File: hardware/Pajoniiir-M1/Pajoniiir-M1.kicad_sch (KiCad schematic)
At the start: 0 parts

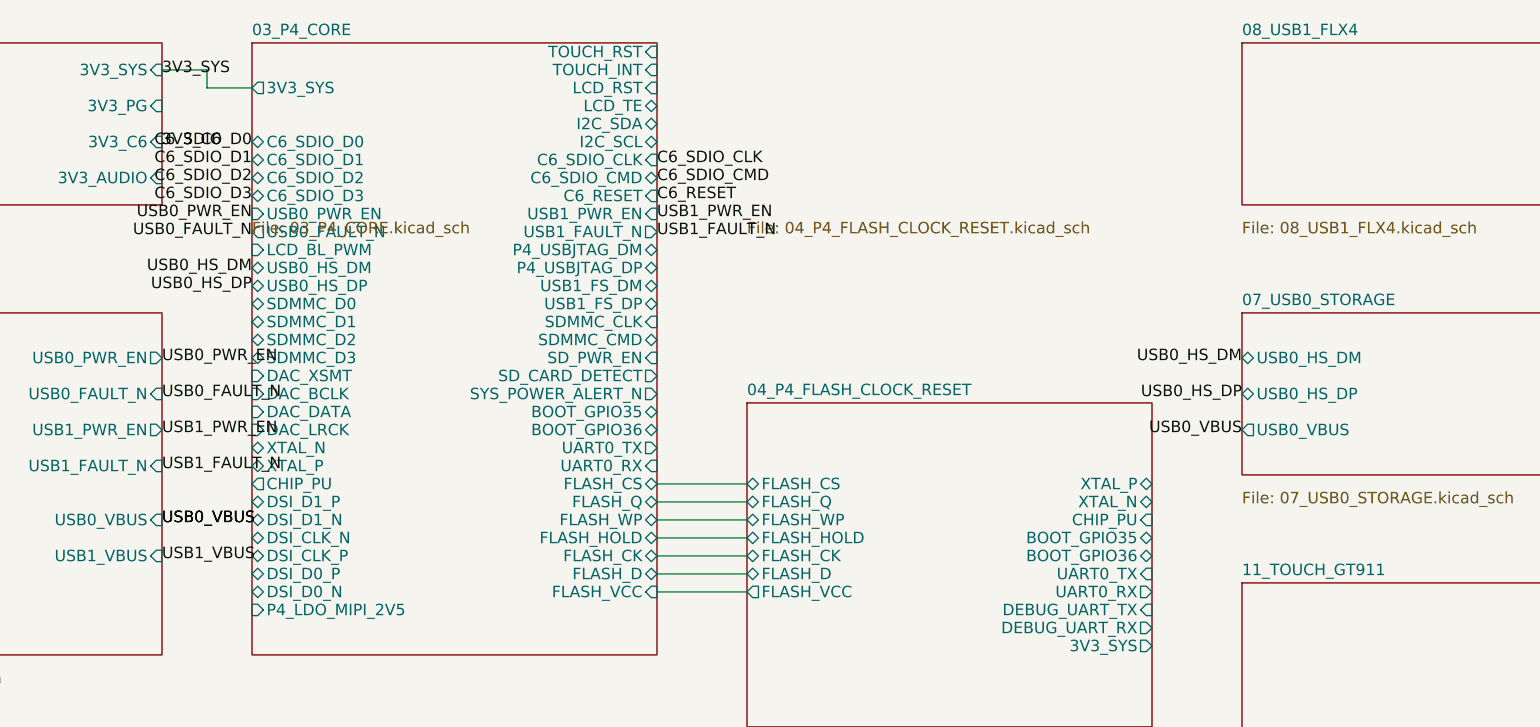
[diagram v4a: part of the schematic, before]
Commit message: hardware: wire USB1 FLX4 hierarchy
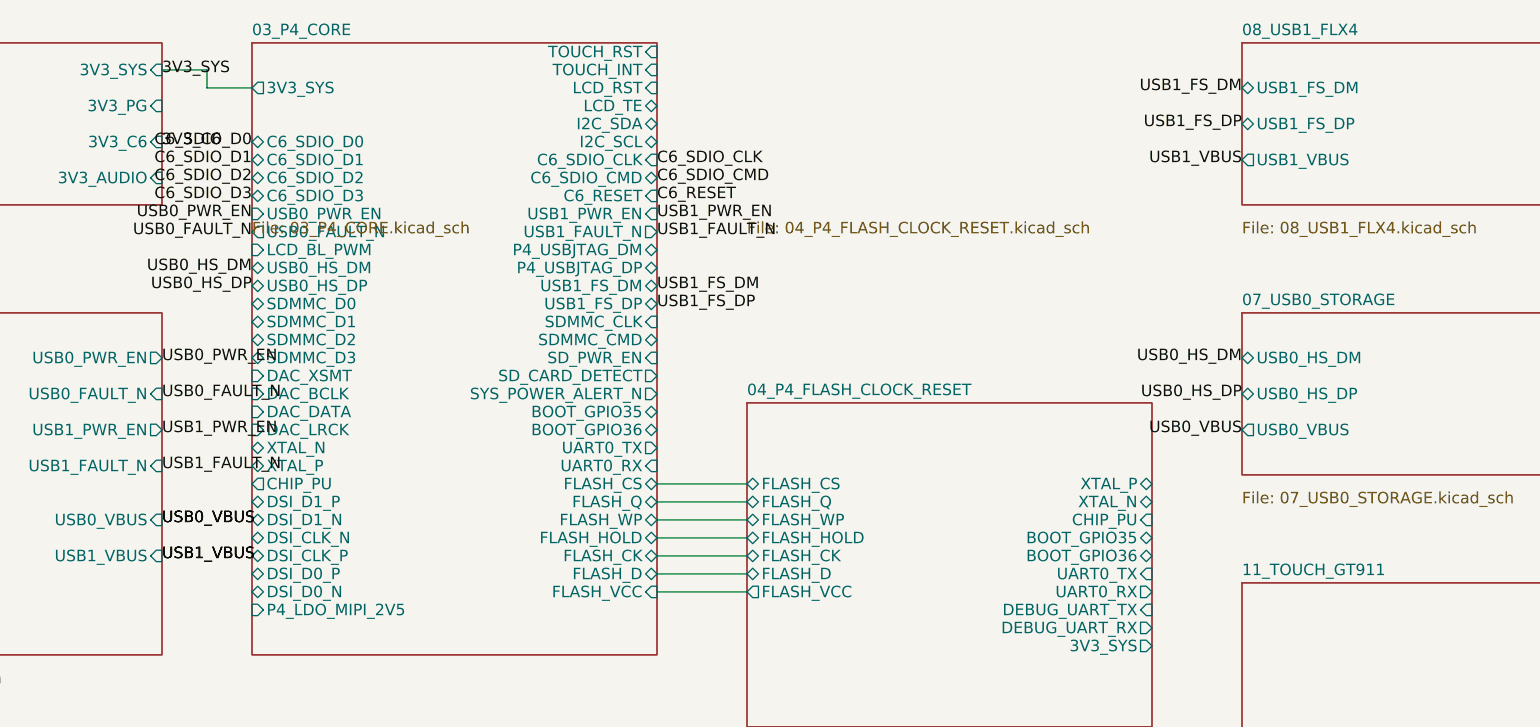
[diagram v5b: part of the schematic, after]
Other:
- sheet 08_USB1_FLX4 ports: added USB1_FS_DM, USB1_FS_DP, USB1_VBUS; removed none
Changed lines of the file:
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@@
       (effects (font (size 1.27 1.27)) (justify left top))
     )
+    (pin "USB1_FS_DM" bidirectional (at 240 25 180) (effects (font (size 1.27 1.27)) (justify left)))
+    (pin "USB1_FS_DP" bidirectional (at 240 29 180) (effects (font (size 1.27 1.27)) (justify left)))
+    (pin "USB1_VBUS" output (at 240 33 180) (effects (font (size 1.27 1.27)) (justify left)))
     (instances
       (project "Pajoniiir-M1"
@@
   (label "USB0_HS_DP" (at 130 47 180) (effects (font (size 1.27 1.27))))
   (label "USB0_VBUS" (at 120 73 0) (effects (font (size 1.27 1.27))))
+  (label "USB1_FS_DM" (at 240 25 180) (effects (font (size 1.27 1.27))))
+  (label "USB1_FS_DP" (at 240 29 180) (effects (font (size 1.27 1.27))))
+  (label "USB1_VBUS" (at 240 33 180) (effects (font (size 1.27 1.27))))
+  (label "USB1_FS_DM" (at 175 47 0) (effects (font (size 1.27 1.27))))
+  (label "USB1_FS_DP" (at 175 49 0) (effects (font (size 1.27 1.27))))
+  (label "USB1_VBUS" (at 120 77 0) (effects (font (size 1.27 1.27))))
   (sheet_instances (path "/" (page "1")))
   (embedded_fonts no)

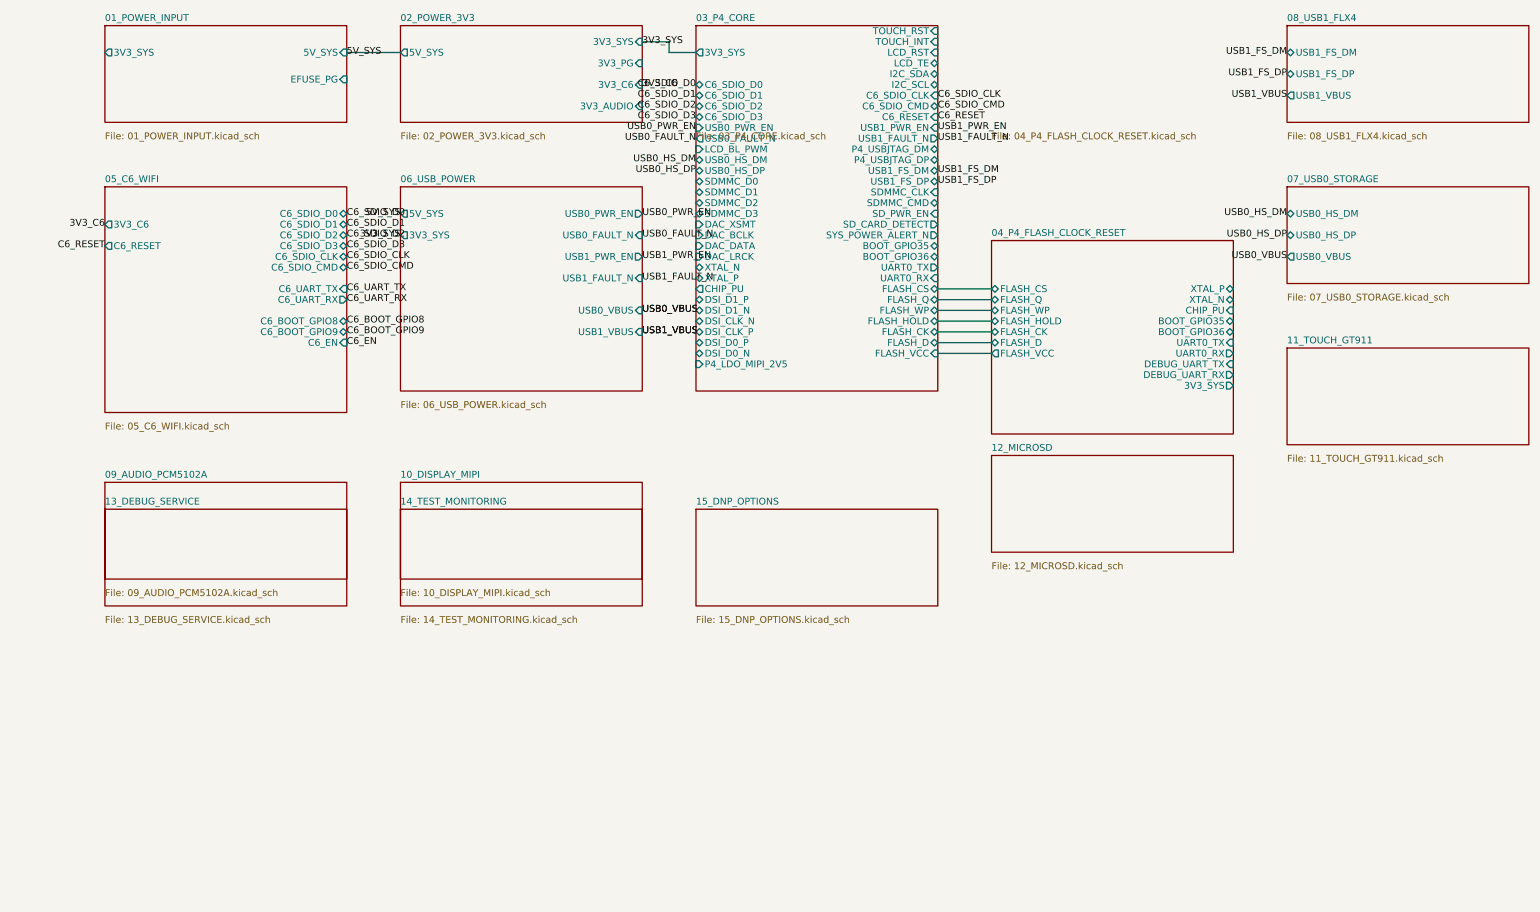
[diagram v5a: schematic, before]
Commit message: hardware: wire audio hierarchy and clean root layout
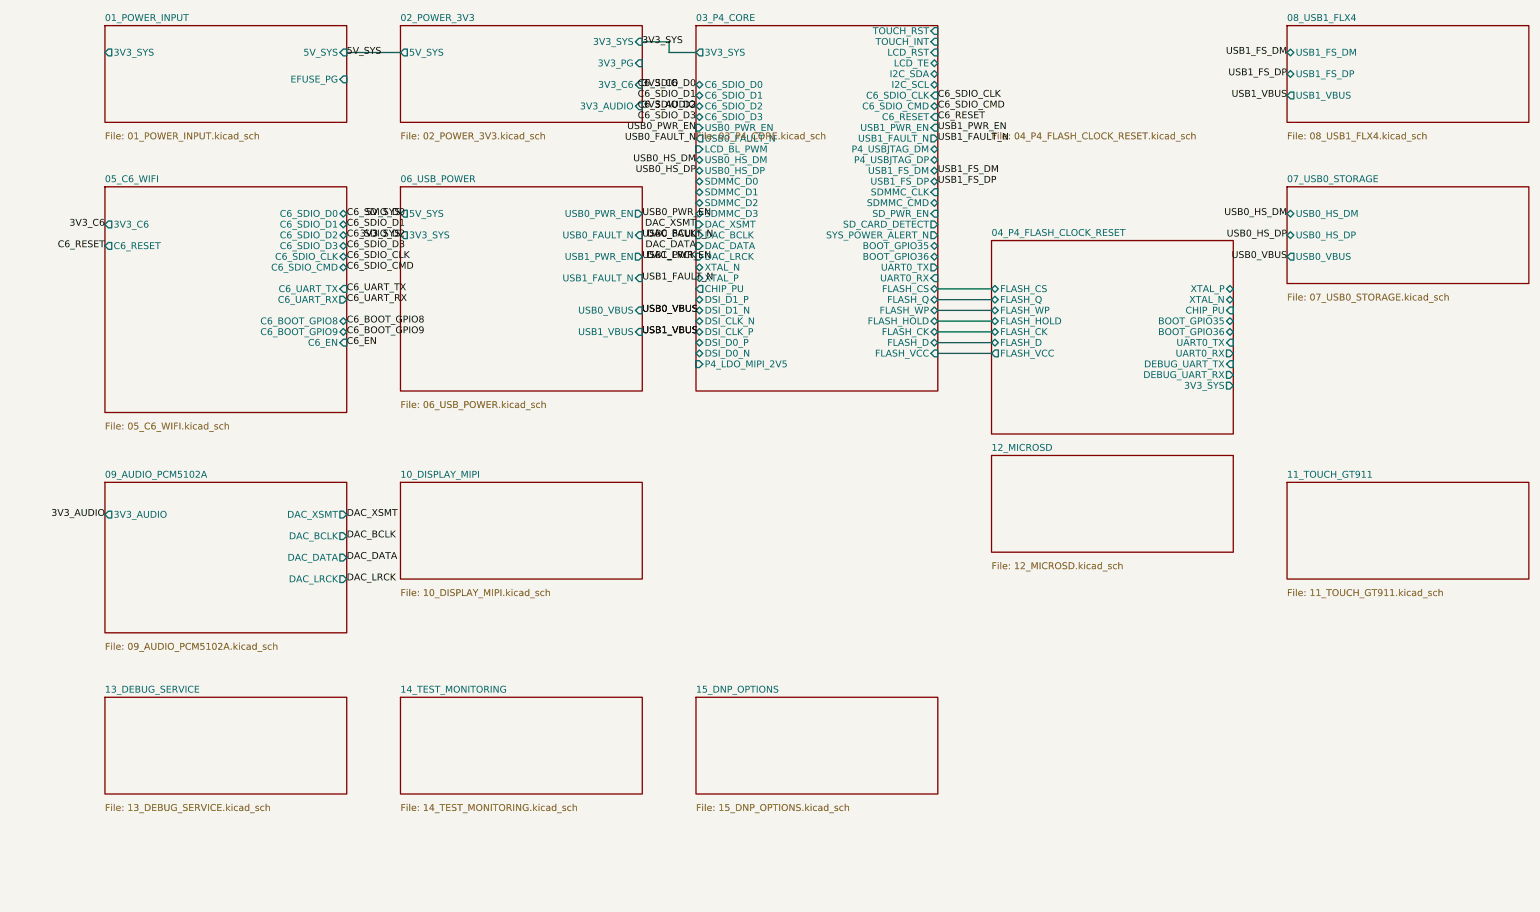
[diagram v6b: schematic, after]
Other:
- sheet 09_AUDIO_PCM5102A ports: added 3V3_AUDIO, DAC_BCLK, DAC_DATA, DAC_LRCK, DAC_XSMT; removed none
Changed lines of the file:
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@@
   (generator "eeschema")
   (generator_version "9.0")
-  (paper "A4")
+  (paper "A3")
   (title_block
     (title "Pajoniiir-M1 Rev A Mainboard")
@@
   (sheet
     (at 20 105)
-    (size 45 18)
+    (size 45 28)
     (fields_autoplaced yes)
     (stroke (width 0.1524) (type solid))
@@
     )
     (property "Sheetfile" "09_AUDIO_PCM5102A.kicad_sch"
-      (at 20 124.8246 0)
-      (effects (font (size 1.27 1.27)) (justify left top))
-    )
+      (at 20 134.8246 0)
+      (effects (font (size 1.27 1.27)) (justify left top))
+    )
+    (pin "3V3_AUDIO" output (at 20 111 180) (effects (font (size 1.27 1.27)) (justify left)))
+    (pin "DAC_XSMT" output (at 65 111 0) (effects (font (size 1.27 1.27)) (justify right)))
+    (pin "DAC_BCLK" output (at 65 115 0) (effects (font (size 1.27 1.27)) (justify right)))
+    (pin "DAC_DATA" output (at 65 119 0) (effects (font (size 1.27 1.27)) (justify right)))
+    (pin "DAC_LRCK" output (at 65 123 0) (effects (font (size 1.27 1.27)) (justify right)))
     (instances
       (project "Pajoniiir-M1"
@@
   )
   (sheet
-    (at 240 80)
+    (at 240 105)
     (size 45 18)
     (fields_autoplaced yes)
@@
     (fill (color 0 0 0 0.0000))
     (property "Sheetname" "11_TOUCH_GT911"
-      (at 240 79.2888 0)
+      (at 240 104.2888 0)
       (effects (font (size 1.27 1.27)) (justify left bottom))
     )
     (property "Sheetfile" "11_TOUCH_GT911.kicad_sch"
-      (at 240 99.8246 0)
+      (at 240 124.8246 0)
       (effects (font (size 1.27 1.27)) (justify left top))
     )
@@
   )
   (sheet
-    (at 20 110)
+    (at 20 145)
     (size 45 18)
     (fields_autoplaced yes)
@@
     (fill (color 0 0 0 0.0000))
     (property "Sheetname" "13_DEBUG_SERVICE"
-      (at 20 109.2888 0)
+      (at 20 144.2888 0)
       (effects (font (size 1.27 1.27)) (justify left bottom))
     )
     (property "Sheetfile" "13_DEBUG_SERVICE.kicad_sch"
-      (at 20 129.8246 0)
+      (at 20 164.8246 0)
       (effects (font (size 1.27 1.27)) (justify left top))
     )
@@
   )
   (sheet
-    (at 75 110)
+    (at 75 145)
     (size 45 18)
     (fields_autoplaced yes)
@@
     (fill (color 0 0 0 0.0000))
     (property "Sheetname" "14_TEST_MONITORING"
-      (at 75 109.2888 0)
+      (at 75 144.2888 0)
       (effects (font (size 1.27 1.27)) (justify left bottom))
     )
     (property "Sheetfile" "14_TEST_MONITORING.kicad_sch"
-      (at 75 129.8246 0)
+      (at 75 164.8246 0)
       (effects (font (size 1.27 1.27)) (justify left top))
     )
@@
   )
   (sheet
-    (at 130 110)
+    (at 130 145)
     (size 45 18)
     (fields_autoplaced yes)
@@
     (fill (color 0 0 0 0.0000))
     (property "Sheetname" "15_DNP_OPTIONS"
-      (at 130 109.2888 0)
+      (at 130 144.2888 0)
       (effects (font (size 1.27 1.27)) (justify left bottom))
     )
     (property "Sheetfile" "15_DNP_OPTIONS.kicad_sch"
-      (at 130 129.8246 0)
+      (at 130 164.8246 0)
       (effects (font (size 1.27 1.27)) (justify left top))
     )
@@
   (label "USB1_FS_DP" (at 175 49 0) (effects (font (size 1.27 1.27))))
   (label "USB1_VBUS" (at 120 77 0) (effects (font (size 1.27 1.27))))
+  (label "3V3_AUDIO" (at 20 111 180) (effects (font (size 1.27 1.27))))
+  (label "DAC_XSMT" (at 65 111 0) (effects (font (size 1.27 1.27))))
+  (label "DAC_BCLK" (at 65 115 0) (effects (font (size 1.27 1.27))))
+  (label "DAC_DATA" (at 65 119 0) (effects (font (size 1.27 1.27))))
+  (label "DAC_LRCK" (at 65 123 0) (effects (font (size 1.27 1.27))))
+  (label "3V3_AUDIO" (at 120 35 0) (effects (font (size 1.27 1.27))))
+  (label "DAC_XSMT" (at 130 57 180) (effects (font (size 1.27 1.27))))
+  (label "DAC_BCLK" (at 130 59 180) (effects (font (size 1.27 1.27))))
+  (label "DAC_DATA" (at 130 61 180) (effects (font (size 1.27 1.27))))
+  (label "DAC_LRCK" (at 130 63 180) (effects (font (size 1.27 1.27))))
   (sheet_instances (path "/" (page "1")))
   (embedded_fonts no)

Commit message: hardware: wire microSD SDMMC hierarchy
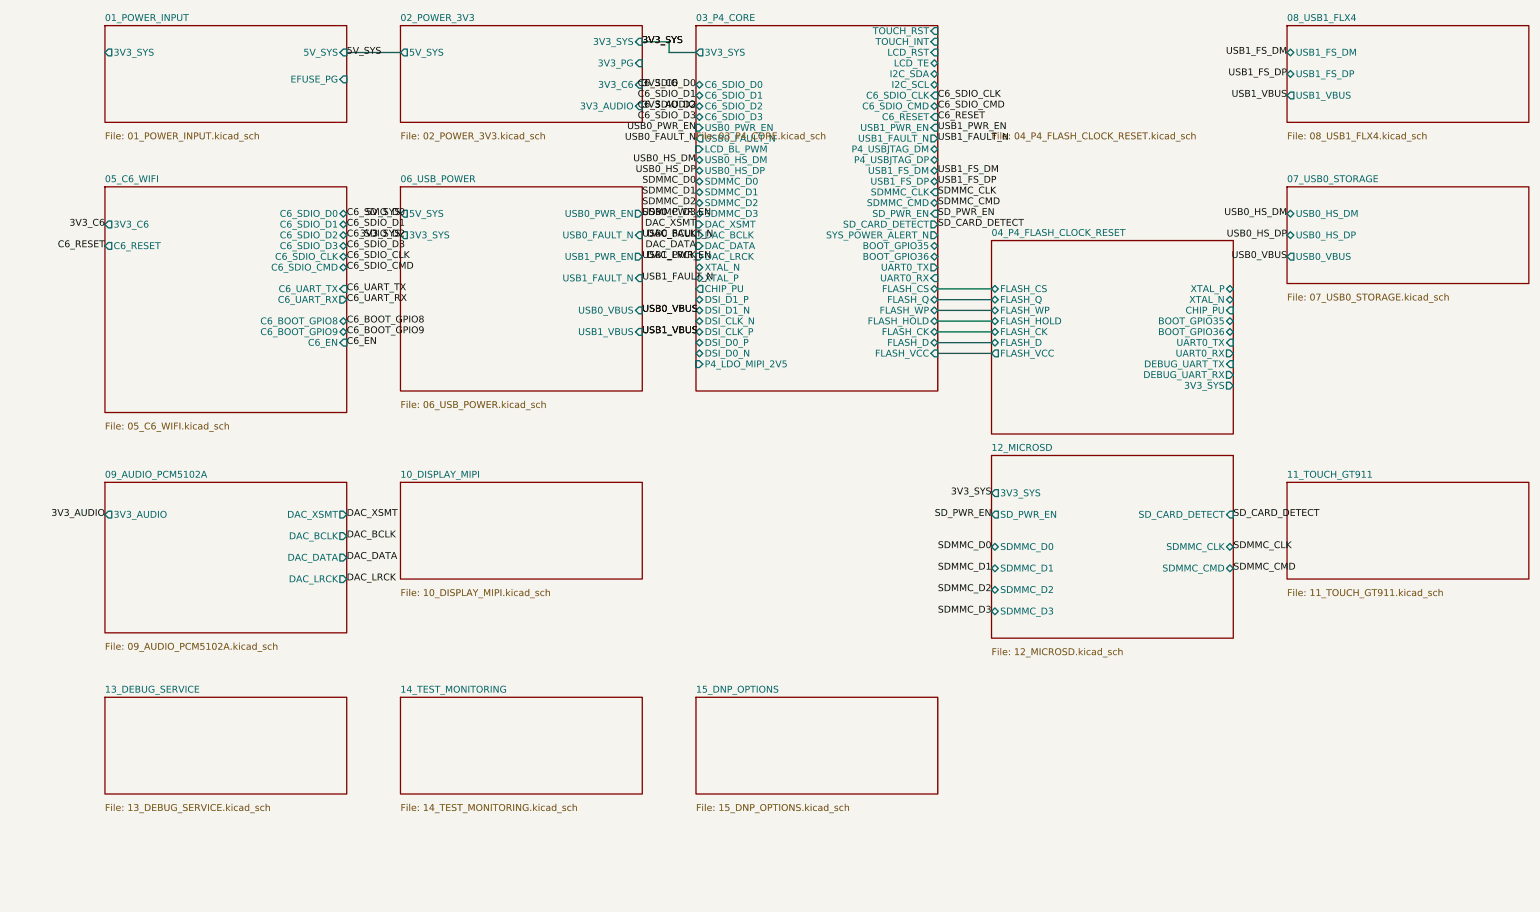
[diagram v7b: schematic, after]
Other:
- sheet 12_MICROSD ports: added 3V3_SYS, SDMMC_CLK, SDMMC_CMD, SDMMC_D0, SDMMC_D1, SDMMC_D2, SDMMC_D3, SD_CARD_DETECT, SD_PWR_EN; removed none
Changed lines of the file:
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@@
   (sheet
     (at 185 100)
-    (size 45 18)
+    (size 45 34)
     (fields_autoplaced yes)
     (stroke (width 0.1524) (type solid))
@@
     )
     (property "Sheetfile" "12_MICROSD.kicad_sch"
-      (at 185 119.8246 0)
+      (at 185 135.8246 0)
       (effects (font (size 1.27 1.27)) (justify left top))
     )
+    (pin "3V3_SYS" output (at 185 107 180) (effects (font (size 1.27 1.27)) (justify left)))
+    (pin "SD_PWR_EN" output (at 185 111 180) (effects (font (size 1.27 1.27)) (justify left)))
+    (pin "SD_CARD_DETECT" input (at 230 111 0) (effects (font (size 1.27 1.27)) (justify right)))
+    (pin "SDMMC_D0" bidirectional (at 185 117 180) (effects (font (size 1.27 1.27)) (justify left)))
+    (pin "SDMMC_D1" bidirectional (at 185 121 180) (effects (font (size 1.27 1.27)) (justify left)))
+    (pin "SDMMC_D2" bidirectional (at 185 125 180) (effects (font (size 1.27 1.27)) (justify left)))
+    (pin "SDMMC_D3" bidirectional (at 185 129 180) (effects (font (size 1.27 1.27)) (justify left)))
+    (pin "SDMMC_CLK" bidirectional (at 230 117 0) (effects (font (size 1.27 1.27)) (justify right)))
+    (pin "SDMMC_CMD" bidirectional (at 230 121 0) (effects (font (size 1.27 1.27)) (justify right)))
     (instances
       (project "Pajoniiir-M1"
@@
   (label "DAC_DATA" (at 130 61 180) (effects (font (size 1.27 1.27))))
   (label "DAC_LRCK" (at 130 63 180) (effects (font (size 1.27 1.27))))
+  (label "3V3_SYS" (at 185 107 180) (effects (font (size 1.27 1.27))))
+  (label "SD_PWR_EN" (at 185 111 180) (effects (font (size 1.27 1.27))))
+  (label "SD_CARD_DETECT" (at 230 111 0) (effects (font (size 1.27 1.27))))
+  (label "SDMMC_D0" (at 185 117 180) (effects (font (size 1.27 1.27))))
+  (label "SDMMC_D1" (at 185 121 180) (effects (font (size 1.27 1.27))))
+  (label "SDMMC_D2" (at 185 125 180) (effects (font (size 1.27 1.27))))
+  (label "SDMMC_D3" (at 185 129 180) (effects (font (size 1.27 1.27))))
+  (label "SDMMC_CLK" (at 230 117 0) (effects (font (size 1.27 1.27))))
+  (label "SDMMC_CMD" (at 230 121 0) (effects (font (size 1.27 1.27))))
+  (label "3V3_SYS" (at 120 23 0) (effects (font (size 1.27 1.27))))
+  (label "SD_PWR_EN" (at 175 55 0) (effects (font (size 1.27 1.27))))
+  (label "SD_CARD_DETECT" (at 175 57 0) (effects (font (size 1.27 1.27))))
+  (label "SDMMC_D0" (at 130 49 180) (effects (font (size 1.27 1.27))))
+  (label "SDMMC_D1" (at 130 51 180) (effects (font (size 1.27 1.27))))
+  (label "SDMMC_D2" (at 130 53 180) (effects (font (size 1.27 1.27))))
+  (label "SDMMC_D3" (at 130 55 180) (effects (font (size 1.27 1.27))))
+  (label "SDMMC_CLK" (at 175 51 0) (effects (font (size 1.27 1.27))))
+  (label "SDMMC_CMD" (at 175 53 0) (effects (font (size 1.27 1.27))))
   (sheet_instances (path "/" (page "1")))
   (embedded_fonts no)
